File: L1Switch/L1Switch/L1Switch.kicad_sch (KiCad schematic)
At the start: 0 parts

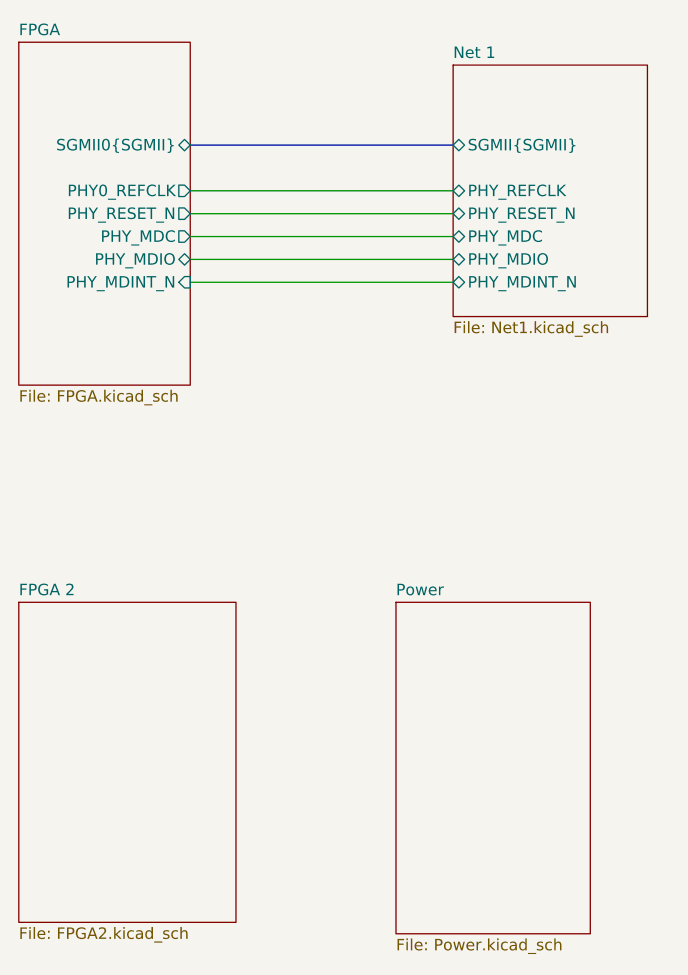
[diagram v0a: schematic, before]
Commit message: Connect/route 8 ports to PHY.
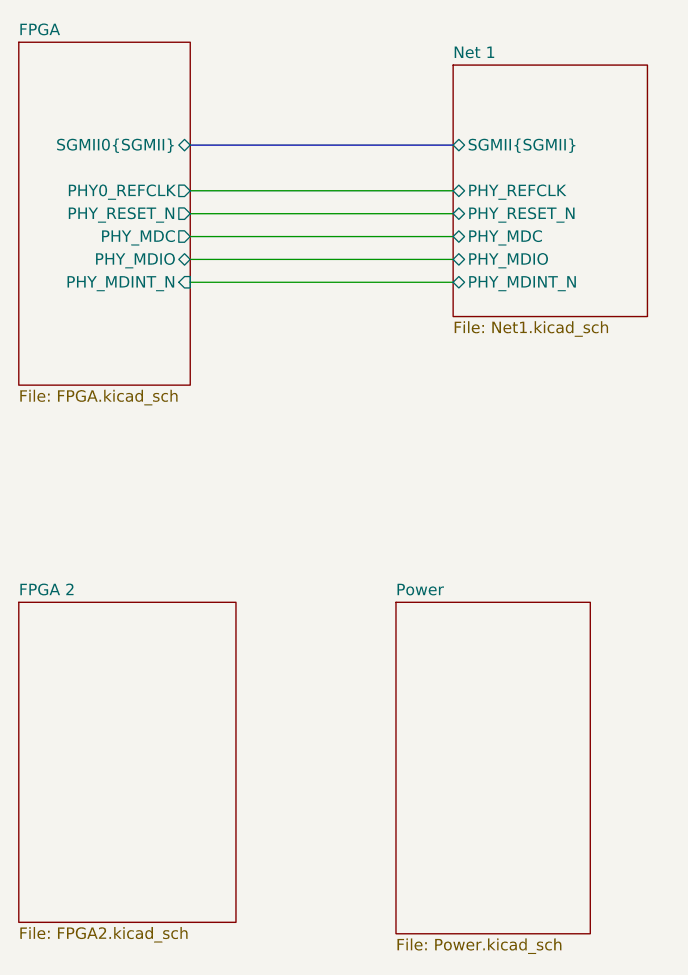
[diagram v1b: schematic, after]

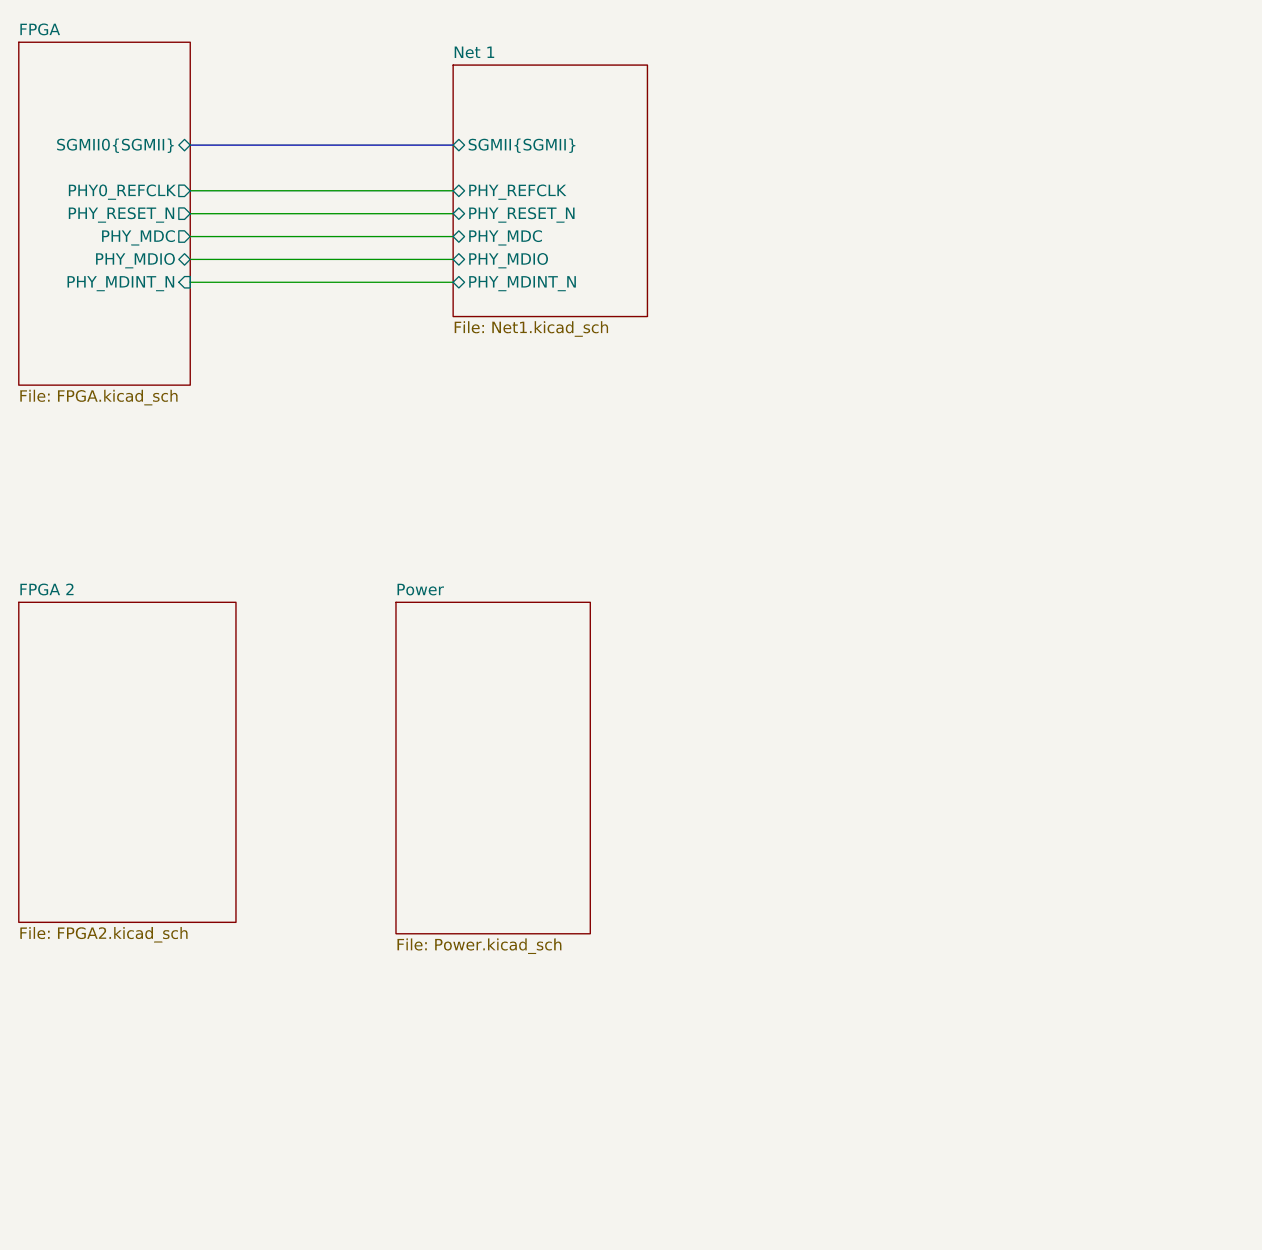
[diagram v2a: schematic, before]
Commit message: Layout replicated to Net2.
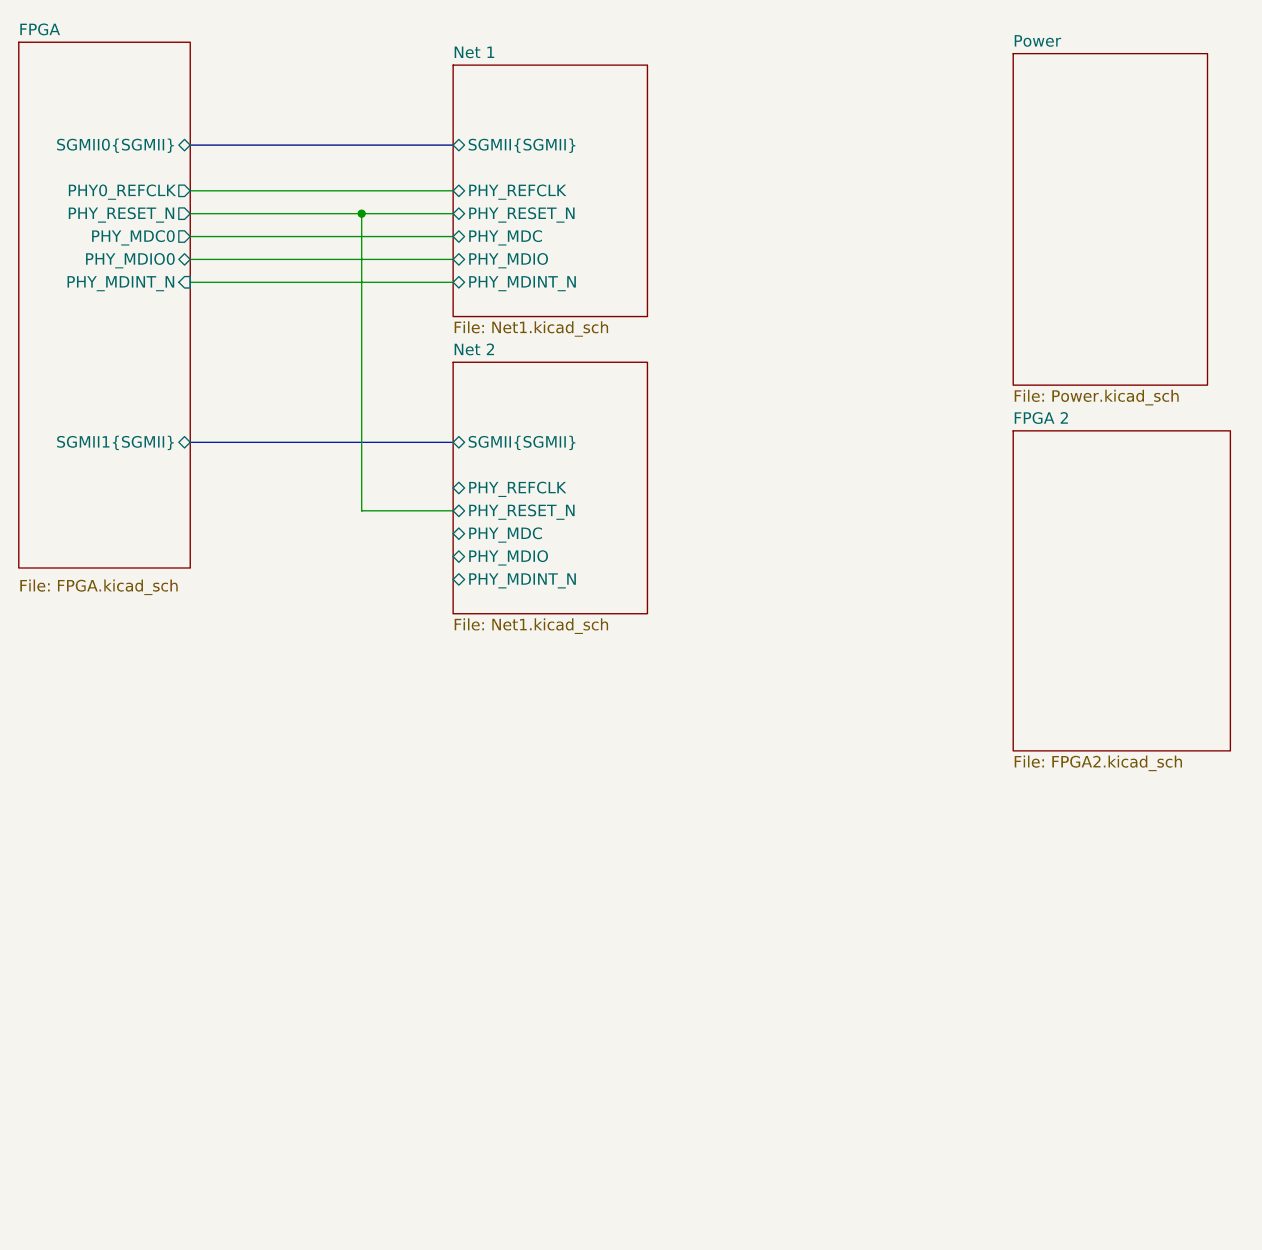
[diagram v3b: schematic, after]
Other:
- added sheet Net 2 (Net1.kicad_sch)
- sheet FPGA ports: added PHY_MDC0, PHY_MDIO0, SGMII1{SGMII}; removed PHY_MDC, PHY_MDIO

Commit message: Add instance 3 and 4 of the network ports.
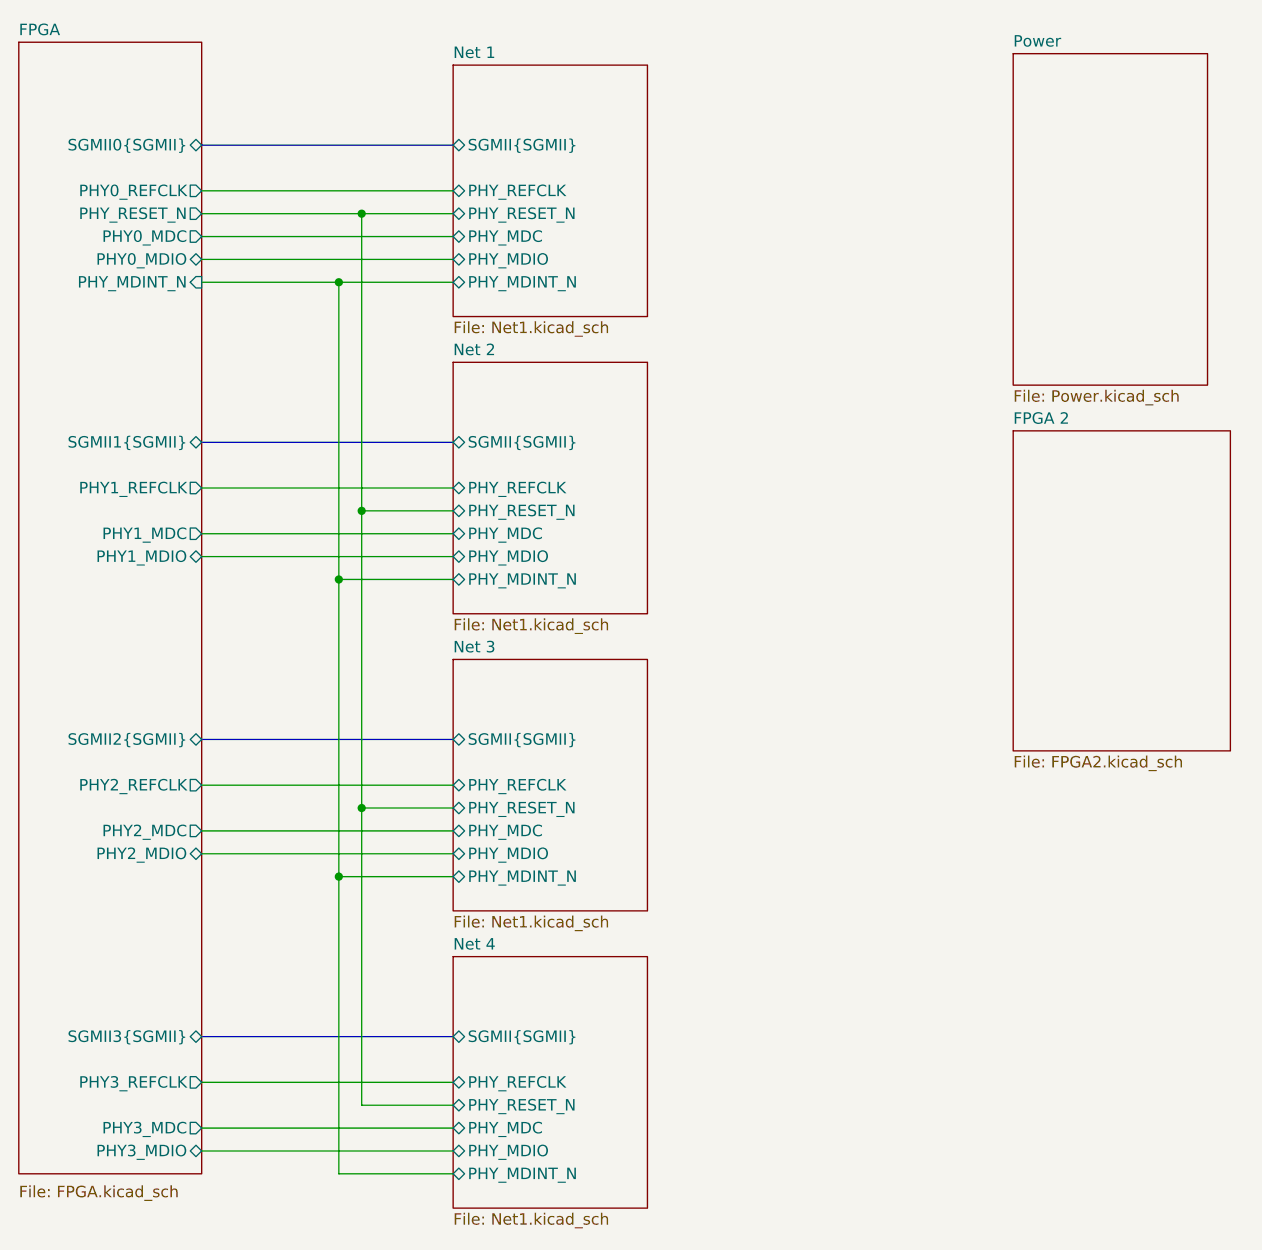
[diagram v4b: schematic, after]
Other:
- added sheet Net 3 (Net1.kicad_sch)
- added sheet Net 4 (Net1.kicad_sch)
- sheet FPGA ports: added PHY0_MDC, PHY0_MDIO, PHY1_MDC, PHY1_MDIO, PHY1_REFCLK, PHY2_MDC, PHY2_MDIO, PHY2_REFCLK, PHY3_MDC, PHY3_MDIO, PHY3_REFCLK, SGMII2{SGMII}, SGMII3{SGMII}; removed PHY_MDC0, PHY_MDIO0
